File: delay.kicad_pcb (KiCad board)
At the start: 2 copper layers, 70 x 90 mm, 56 parts, among them J1 Footswitch_Terminal_01x02, J2 LED_Socket_01x02, J3 Footswitch_Terminal_Signal_01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, J4 Power_Supply_Terminal_01x02, J5 IO_Ground_Terminal_01x02, U1 L7805, U2 TL072, U3 PT2399

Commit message: update pcb design
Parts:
- moved C3 9.67 mm to (148.6, 97.8), turned to -90 degrees
- moved C4 7.62 mm to (162.0, 109.7), turned to -90 degrees
- moved C13 6.04 mm to (161.5, 90.9)
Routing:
- net 0: track 46.5 -> 33.2 mm, vias 13 -> 14
- net Net-(U3-REF): track 6.80 -> 10.4 mm
- net /REG_OUT: track 32.4 -> 29.0 mm
- net /+LED: track 76.3 -> 73.1 mm
- net Net-(C5-Pad2): track 0.00 -> 2.43 mm

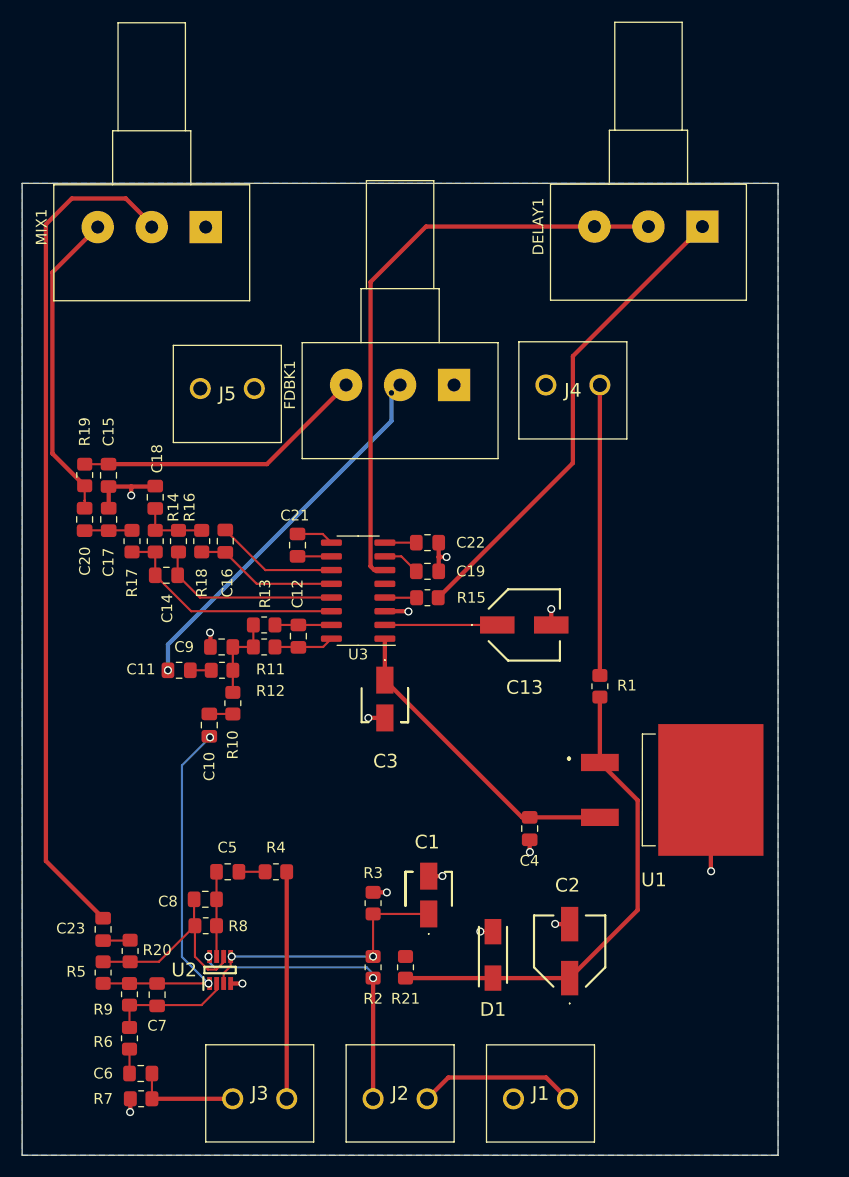
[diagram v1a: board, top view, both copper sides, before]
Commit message: add ground vias inside stabilisator GND field, add board revision info
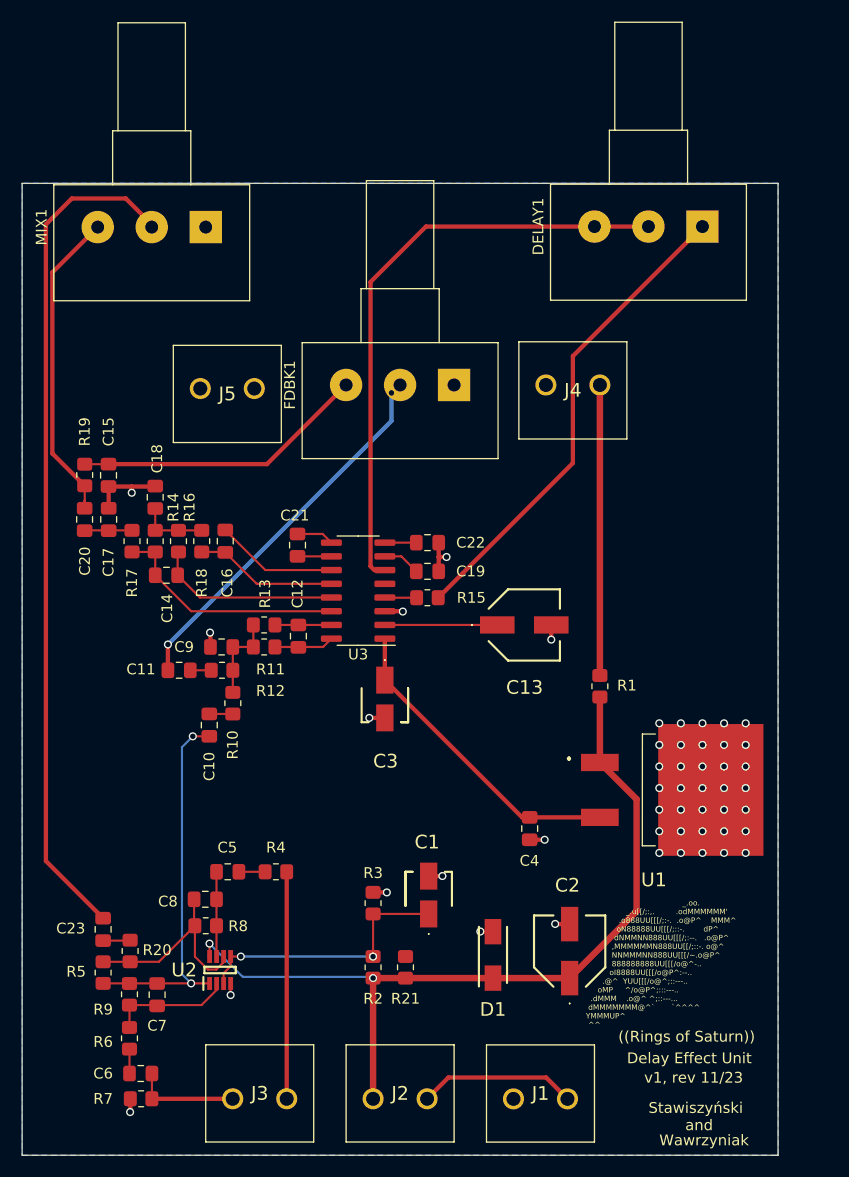
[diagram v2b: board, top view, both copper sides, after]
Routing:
- net 0: track 33.2 -> 24.9 mm, vias 14 -> 48
- net /+LED: track 73.1 -> 77.1 mm
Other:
- board text added: "((Rings of Saturn))"
- board text added: "Delay Effect Unit"
- board text added: "Stawiszyński"
- board text added: "Wawrzyniak"
- board text added: "_.oo. _.u[[/;:,. .odMMMMMM' .o888UU[[[/;:-. .o@P^ MMM^ oN88888UU[[[/;::-. dP^ dNMMNN888UU[[[/;:--. .o@P^ ,MMMMMMN888UU[[/;::-. o@^ NNMMMNN888UU[[[/~.o@P^ 888888888UU[[[/o@^-.. oI8888UU[[[/o@P^:--.. .@^ YUU[[[/o@^;::---.. oMP ^/o@P^;:::---.. .dMMM .o@^ ^;::---... dMMMMMMM@^` `^^^^ YMMMUP^ ^^"
- board text added: "and"
- board text added: "v1, rev 11/23"

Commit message: improve ground plane design, add thicker routes to audio paths
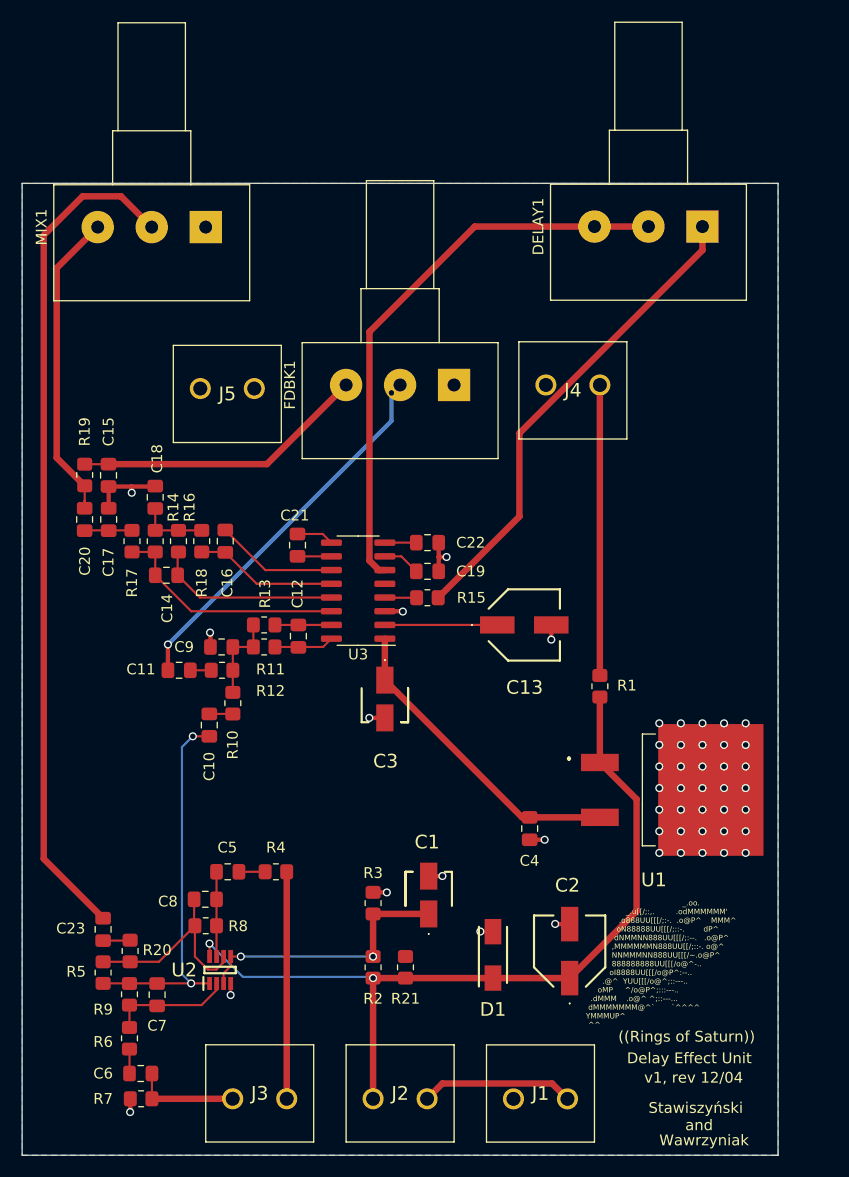
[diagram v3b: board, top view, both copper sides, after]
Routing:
- net Net-(U3-VCO): track 55.7 -> 54.0 mm
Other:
- board text added: "v1, rev 12/04"
- board text removed: "v1, rev 11/23"

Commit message: refactor pcb design, reduce board size to 70x70
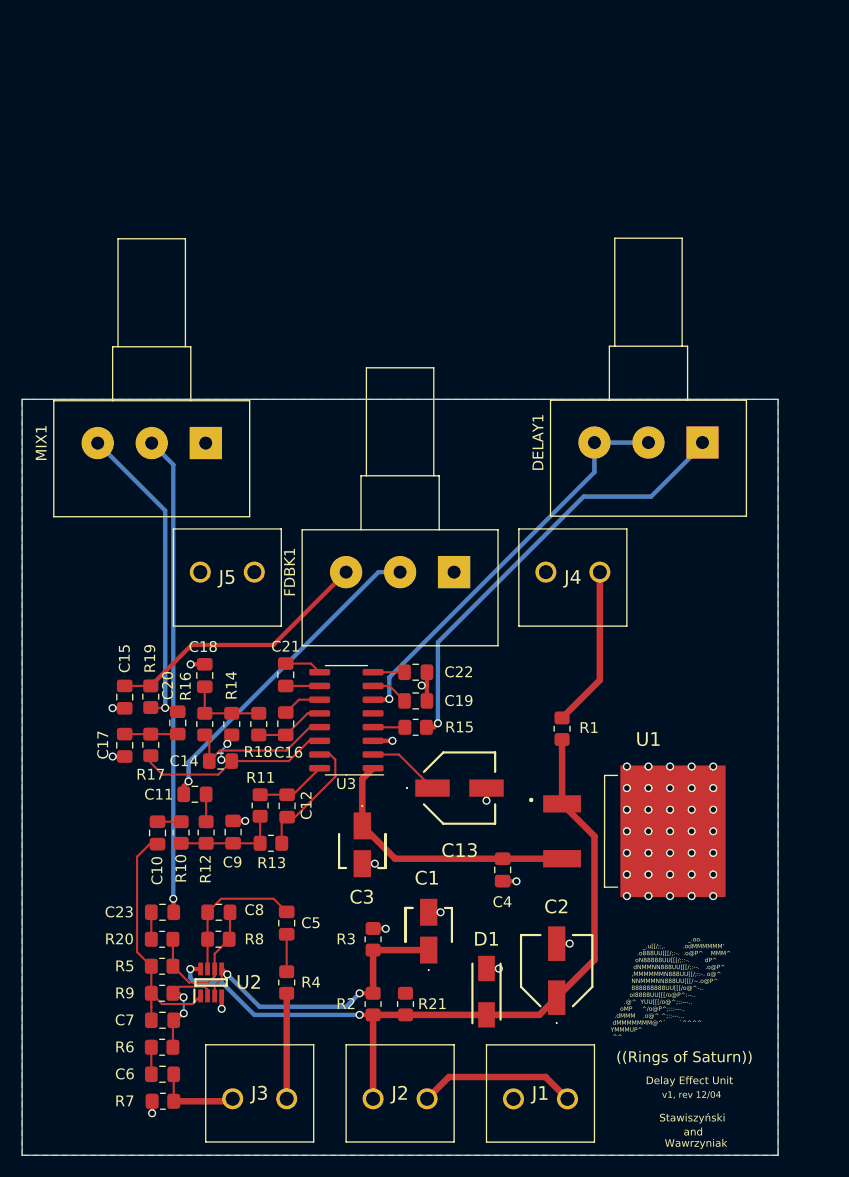
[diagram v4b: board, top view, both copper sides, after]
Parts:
- moved R19 21.4 mm to (126.9, 97.5)
- moved C17 21.0 mm to (124.5, 102.0), turned to 90 degrees
- moved C20 20.7 mm to (129.4, 100.0)
- moved C15 20.6 mm to (124.5, 97.6)
- moved R13 20.2 mm to (138.0, 111.1)
- moved DELAY1 20.0 mm to (178.0, 74.0)
- moved MIX1 20.0 mm to (132.0, 74.0)
- moved R17 18.9 mm to (126.9, 102.0)
- moved R14 18.4 mm to (134.4, 100.1)
- moved C14 17.9 mm to (133.4, 103.5), turned to 180 degrees
- moved C16 17.8 mm to (139.4, 100.0)
- moved R18 17.7 mm to (136.9, 100.1)
- moved FDBK1 17.3 mm to (155.0, 86.0)
- moved J4 17.3 mm to (168.5, 86.0)
- moved C9 17.2 mm to (134.5, 110.1), turned to 90 degrees
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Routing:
- net Net-(C23-Pad1): track 78.4 -> 44.6 mm, vias 0 -> 1
- net Net-(U3-VCO): track 54.0 -> 38.1 mm, vias 0 -> 1
- net VDD: track 26.9 -> 14.9 mm
- net /SIGNAL_CLEAN: track 35.2 -> 23.4 mm, vias 2 -> 0
- net /OUTPUT: track 21.0 -> 9.77 mm
- net Net-(U3-OP2-IN): track 11.4 -> 3.65 mm
- net Net-(U3-OP2-OUT): track 13.2 -> 6.48 mm
- net Net-(U3-LPF1-OUT): track 5.23 -> 11.9 mm
- net Net-(C5-Pad1): track 7.85 -> 13.6 mm
- net Net-(U2B--): track 19.3 -> 13.7 mm
- net Net-(C11-Pad2): track 35.4 -> 30.0 mm, vias 2 -> 1
- net /+LED: track 77.1 -> 72.1 mm
- net 0: track 24.9 -> 20.2 mm, vias 48 -> 50
- net Net-(U3-REF): track 10.4 -> 6.79 mm
- net /REG_OUT: track 29.0 -> 25.5 mm
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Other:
- board size 70 x 90 mm -> 70 x 70 mm

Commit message: add pcb mounting holes
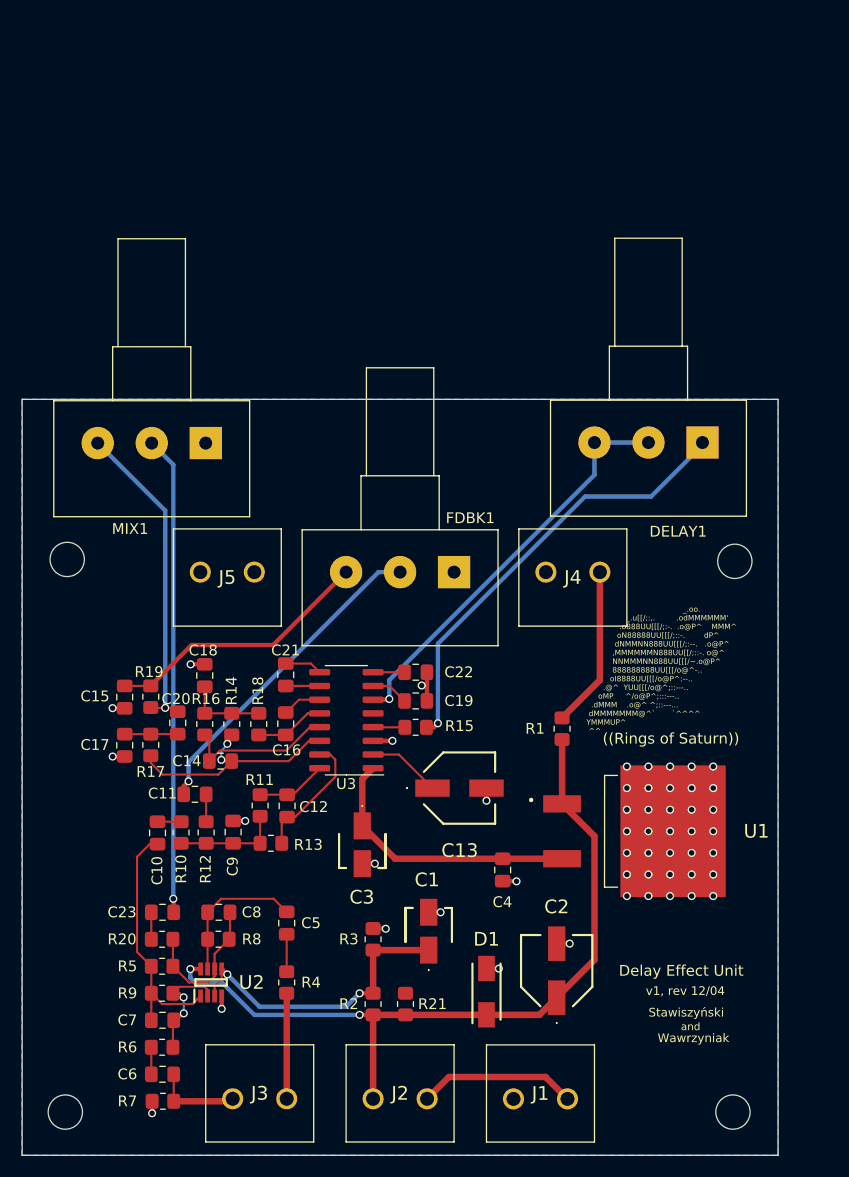
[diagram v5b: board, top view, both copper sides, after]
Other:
- outline, holes or cut-outs redrawn

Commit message: small track thickness and area keepout adjustments
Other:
- board text added: "v1, rev 12/05"
- board text removed: "v1, rev 12/04"
